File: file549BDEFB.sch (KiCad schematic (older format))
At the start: 38 parts, among them IC1 L293D, K3 I2C, SW10 5, SW11 6, SW12 7, SW13 8, SW14 1, SW15 2, SW16 3, SW17 4, SW2 C, SW3 D, SW4 E, SW5 F, SW6 9, SW7 0, SW8 A, SW9 B, U2 24C16, U3 DS1307, U4 BATTERY, X1 CRYSTAL

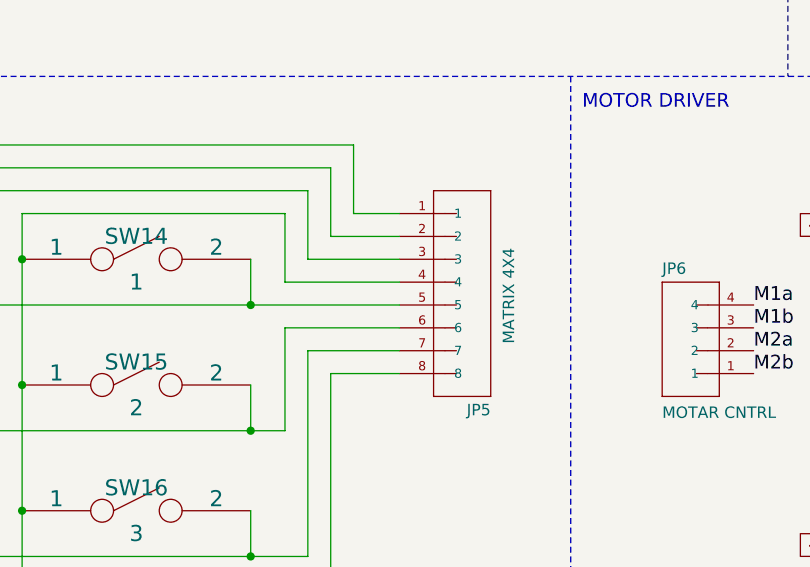
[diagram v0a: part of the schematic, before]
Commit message: Ver1.2
1. Mounting holes for slide switch
2. Nomenclature for all the ident.
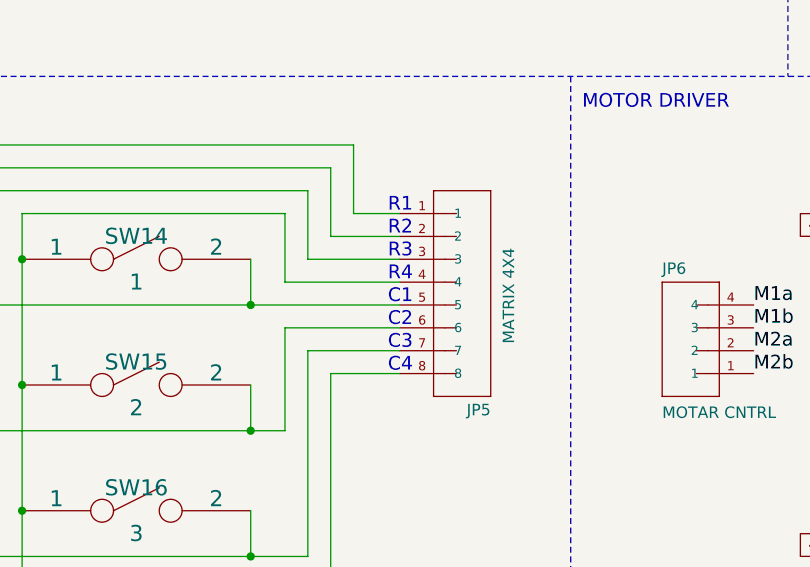
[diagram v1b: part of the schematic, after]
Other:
- note added: "C1"
- note added: "C2"
- note added: "C3"
- note added: "C4"
- note added: "R1"
- note added: "R2"
- note added: "R3"
- note added: "R4"
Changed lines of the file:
@@
 LIBS:valves
 LIBS:Ultra_DB_X51_v1-cache
-EELAYER 27 0
+EELAYER 25 0
 EELAYER END
 $Descr A4 11693 8268
@@
 79 E3 73 01 AA 0D CF 9F 3C 98 C5 F6 CF AC 04 72 85 62 D7 80 77 B1 8B CB 18 6F AC E9 6A 17 BB B8
 C2 B0 6B C0 BB D8 C5 65 8C 5D 03 DE C5 2E 2E 63 EC 1A F0 2E 76 71 19 63 D7 80 77 B1 8B CB 18 BB
-06 BC 8B 5D 5C C6 F8 FF 01 52 B3 1C 8C A4 9D 25 1B 00 00 00 00 49 45 4E 44 AE 42 60 82 25 $EndBitmap
+06 BC 8B 5D 5C C6 F8 FF 01 52 B3 1C 8C A4 9D 25 1B 00 00 00 00 49 45 4E 44 AE 42 60 82 1B
 EndData
 $EndBitmap
+Text Notes 6350 4600 0    60   ~ 0
+R1
+Text Notes 6350 4700 0    60   ~ 0
+R2
+Text Notes 6350 4800 0    60   ~ 0
+R3
+Text Notes 6350 4900 0    60   ~ 0
+R4
+Text Notes 6350 5000 0    60   ~ 0
+C1
+Text Notes 6350 5100 0    60   ~ 0
+C2
+Text Notes 6350 5200 0    60   ~ 0
+C3
+Text Notes 6350 5300 0    60   ~ 0
+C4
 $EndSCHEMATC
